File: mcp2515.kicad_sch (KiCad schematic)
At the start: 10 parts, among them U10 SN65HVD232, U9 MCP2515, Y2 Crystal

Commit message: Added DS1307 RTC and micro SD card
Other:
- title: (none) -> Iron Warriors v2.0 
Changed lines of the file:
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@@
 (kicad_sch (version 20211123) (generator eeschema)
   (paper "A4")
+  (title_block
+    (title "Iron Warriors v2.0 ")
+    (date "2023-07-16")
+    (rev "1.1")
+  )
   (junction (at 176.53 34.29) (diameter 0) (color 0 0 0 0)
   )

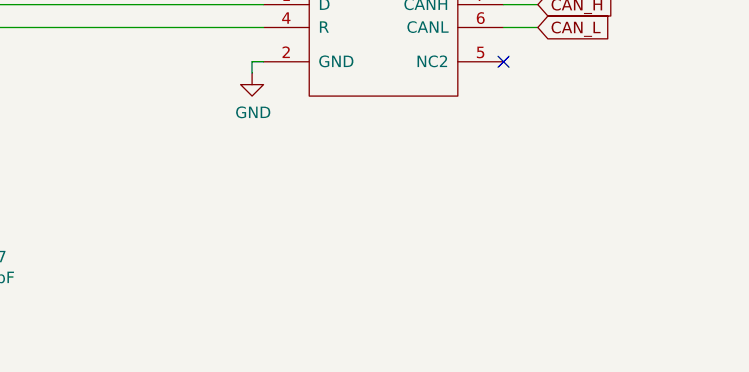
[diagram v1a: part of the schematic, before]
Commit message: Added schematic descriptions
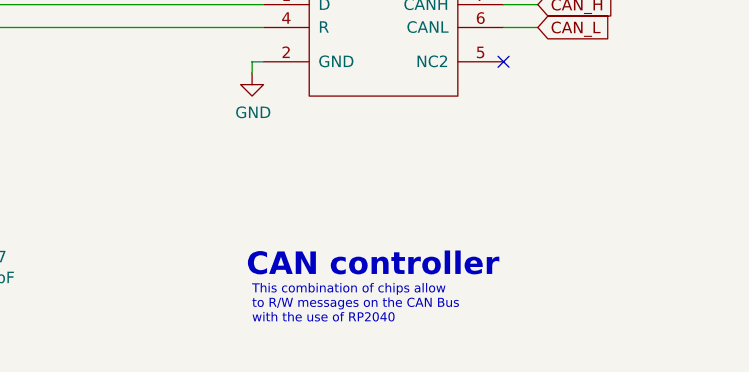
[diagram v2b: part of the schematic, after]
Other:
- note added: "CAN controller"
- note added: "This combination of chips allow to R/W messages on the CAN Bus with the use of RP2040"
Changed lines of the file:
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@@
   (title_block
     (title "Iron Warriors v2.0 ")
-    (date "2023-07-16")
+    (date "2023-08-01")
     (rev "1.1")
   )
@@
     (stroke (width 0) (type default) (color 0 0 0 0))
   )
+  (text "CAN controller\n" (at 222.885 77.47 0)
+    (effects (font (size 2.5 2.5) (thickness 0.254) bold) (justify left bottom))
+  )
+  (text "This combination of chips allow\nto R/W messages on the CAN Bus \nwith the use of RP2040"
+    (at 223.52 82.55 0)
+    (effects (font (size 1 1)) (justify left bottom))
+  )
   (text "connect pin to GND\nto allow usage of SN65HVD230" (at 241.3 27.94 0)

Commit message: Added 12V regulator for injector
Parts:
- removed Y2: Crystal, Crystal:Crystal_SMD_3225-4Pin_3.2x2.5mm, symbol Device:Crystal
- added Y4: Crystal_GND24, symbol Device:Crystal_GND24
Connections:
- net GND: now also Y4.2, Y4.4
- net MCP2515_OSC1: now also Y4.3
- net MCP2515_OSC2: now also Y4.1
